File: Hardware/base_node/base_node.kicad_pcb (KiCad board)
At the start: 2 copper layers, 60 x 60 mm, 29 parts, among them J1 IO Interface, J2 RS-422 Connector, J3 Expantion Connector, J4 I2C, J5 24vdc, J6 Encoder 1, J7 Encoder 2, SW1 SW_DIP_x08, U1 CH32X033F8P6, U2 MAX491E, U3 74HC165, U4 MP1584EN_Module

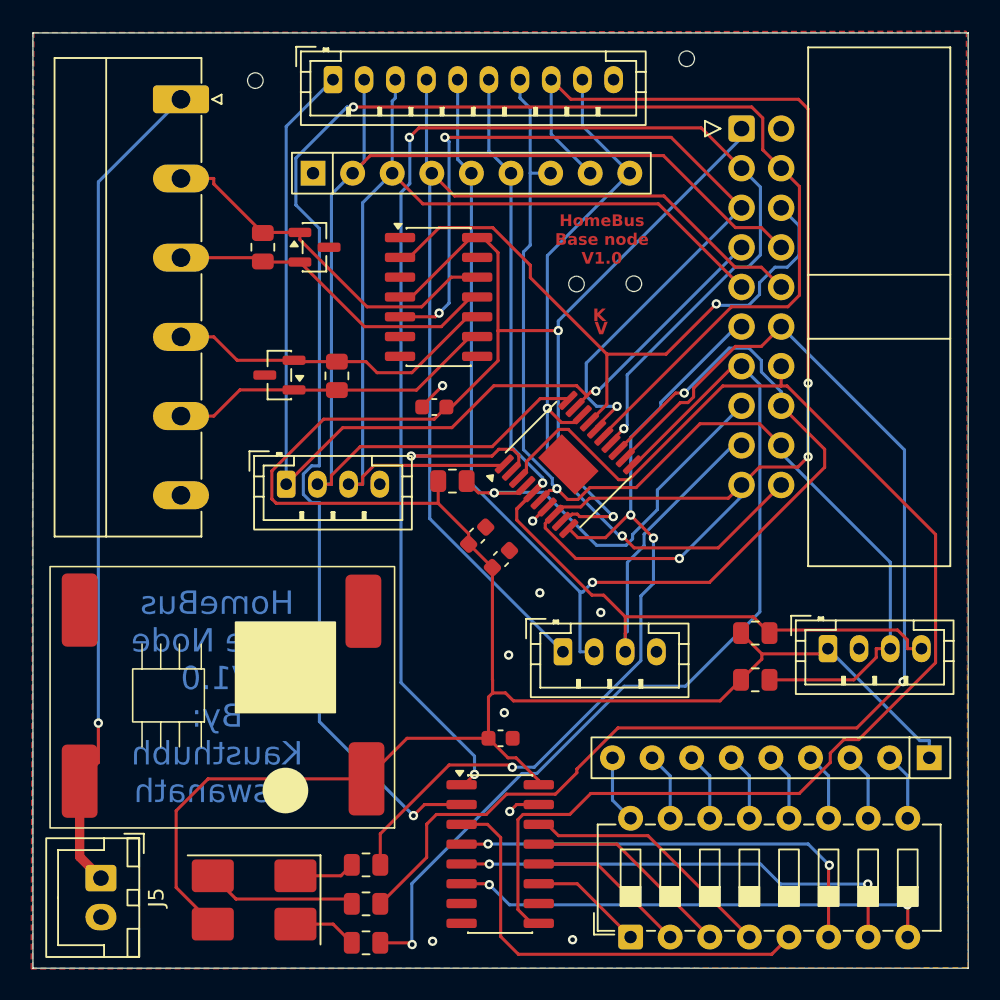
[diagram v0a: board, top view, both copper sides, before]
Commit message: docs: establish hierarchical documentation structure and subsystem guides
- Created root navigation hub README.md linking architecture, subsystems, and components
- Added Hardware Subsystem README (bus topology, 24V power rail, RS-422, SM712 protection, BOM)
- Created Base Node README with pinouts (Dev vs Prod), 3D production renders, and manufacturing specs
- Created Gateway Node README with dual-transceiver room segmentation, EEPROM routing, and dev board
- Created Fan Controller Node README with ZCD optocoupler, isolated gate drive, and anti-stall logic
- Created Expanders README with SMD breakout adapter specs and layout previews
- Created Firmware & Protocol Specification README covering 32-bit addressing, packet formats, and dual-slot OTA
- Synchronized KiCad hardware assets, manufacturing plots, and component libraries
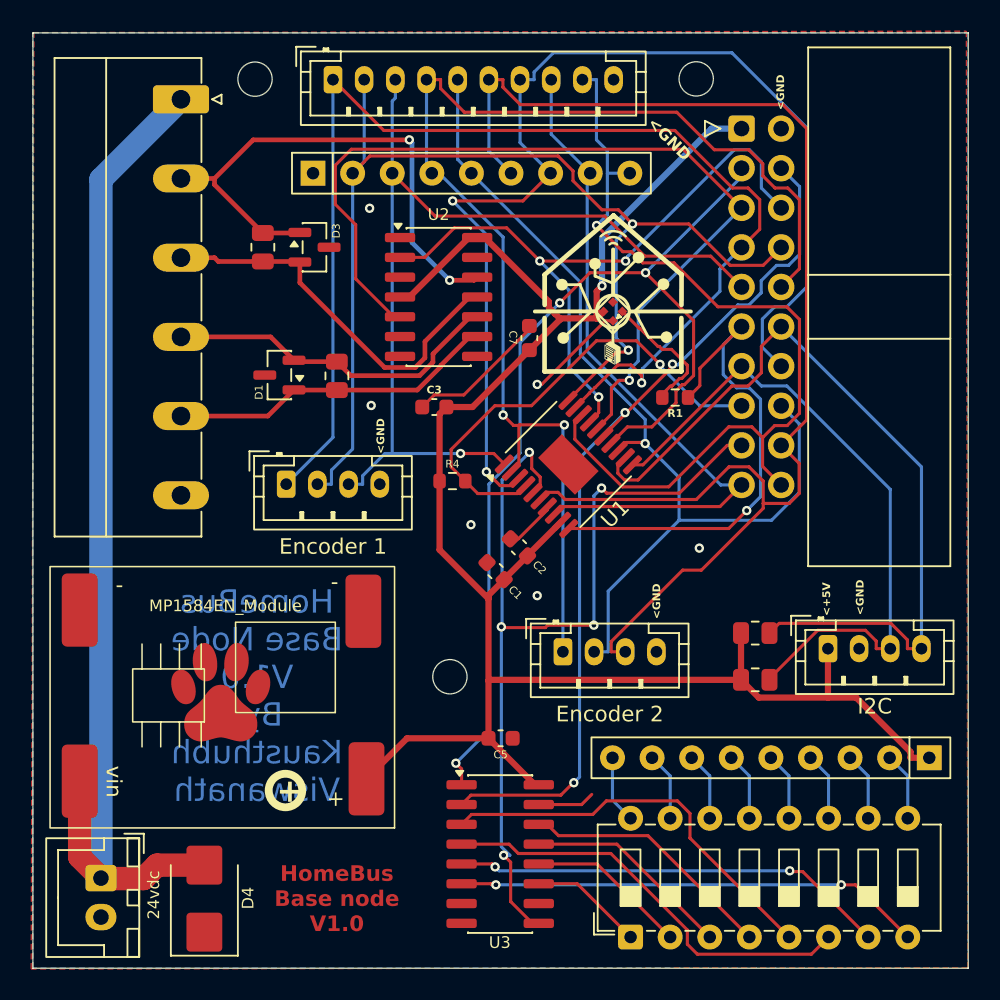
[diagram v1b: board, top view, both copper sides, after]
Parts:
- removed R2, R3: 330Ω, HomeBus:R_0805_2012Metric
- added C7: 100nF, HomeBus:C_0603_1608Metric, F.Cu at (186.3, 115.6)
- added D4: SMBJ26A, Diode_SMD:D_SMB, F.Cu at (165.5, 151.5)
- added Lg1: HomeBus_LOGO, HomeBus:HomeBus_LOGO, F.Cu at (191.7, 113.9)
- added Lg2: OSHW-Logo_5.7x6mm_SilkScreen, Symbol:OSHW-Logo_5.7x6mm_SilkScreen, B.Cu at (168.8, 151.1)
- added Mount1: MountingHole_2.2mm_M2, MountingHole:MountingHole_2.2mm_M2, B.Cu at (168.7, 99.0)
- added Mount2: MountingHole_2.2mm_M2, MountingHole:MountingHole_2.2mm_M2, B.Cu at (197.1, 99.0)
- added Mount3: MountingHole_2.2mm_M2, MountingHole:MountingHole_2.2mm_M2, B.Cu at (181.2, 137.3)
- D2: value LED_RGAB -> WS2812B; footprint HomeBus:Crystal_SMD_0603-4Pin_6.0x3.5mm_HandSoldering -> HomeBus:XINGLIGHT-XL-1010RGBC-WS2812B
- R1, R4: footprint HomeBus:R_0805_2012Metric -> Resistor_SMD:R_0603_1608Metric
- moved D2 44.2 mm to (191.7, 113.9), turned to 45 degrees
- moved R1 35.9 mm to (195.7, 119.4)
- moved C1 2.56 mm to (184.2, 130.5), turned to 135 degrees
- moved C2 1.38 mm to (185.7, 129.0), turned to 135 degrees
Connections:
- net /+24vdc renamed /+24V
- D2 pad 1: Net-(D2-RK) -> +5V
- D2 pad 2: Net-(D2-GK) -> unconnected-(D2-DOUT-Pad2)
- D2 pad 3: +5V -> GND
- D2 pad 4: Net-(D2-BK) -> Net-(D2-DIN)
- J3 pad 12: Net-(J3-Pin_12) -> /SCL
- J3 pad 13: Net-(J3-Pin_13) -> /SDA
- J3 pad 14: Net-(J3-Pin_14) -> Net-(J1-Pin_7)
- J3 pad 17: Net-(J1-Pin_6) -> Net-(J3-Pin_17)
- J3 pad 18: Net-(J1-Pin_7) -> Net-(J1-Pin_6)
- J4 pad 3: Net-(J1-Pin_7) -> /SDA
- J4 pad 4: Net-(J1-Pin_6) -> /SCL
- R1 pad 2: Net-(D2-RK) -> Net-(D2-DIN)
- R7 pad 2: Net-(J1-Pin_7) -> /SDA
- R8 pad 2: Net-(J1-Pin_6) -> /SCL
- U1 pad 11: Net-(J3-Pin_13) -> /SDA
- U1 pad 12: Net-(J3-Pin_12) -> /SCL
- U1 pad 3: Net-(J3-Pin_14) -> Net-(J1-Pin_7)
- U1 pad 5: Net-(J1-Pin_6) -> Net-(J3-Pin_17)
- U1 pad 6: Net-(J1-Pin_7) -> Net-(J1-Pin_6)
- U3 pad 9: Net-(J3-Pin_14) -> Net-(J3-Pin_17)
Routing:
- net Net-(J3-Pin_14): track 84.4 -> 0.00 mm
- net Net-(J3-Pin_12): track 80.7 -> 0.00 mm, vias 1 -> 0
- net Net-(J3-Pin_13): track 61.4 -> 0.00 mm, vias 1 -> 0
- net Net-(J3-Pin_17): track 0.00 -> 61.2 mm, vias 0 -> 5
- net Net-(J3-Pin_4): track 110.4 -> 57.0 mm, vias 2 -> 3
- net /SCL: track 0.00 -> 52.3 mm
- net +5V: track 172.0 -> 123.7 mm, vias 2 -> 1
- net /SDA: track 0.00 -> 42.5 mm
- net Net-(J1-Pin_8): track 82.0 -> 44.8 mm, vias 3 -> 0
- net Net-(J3-Pin_3): track 89.4 -> 64.8 mm
- net Net-(J3-Pin_11): track 53.7 -> 32.0 mm, vias 3 -> 1
- net Net-(J1-Pin_5): track 80.6 -> 61.8 mm, vias 2 -> 1
- net GND: track 5.26 -> 22.7 mm, vias 9 -> 6
- net Net-(J1-Pin_1): track 64.3 -> 78.8 mm
- net /+24V: track 53.2 -> 65.9 mm, vias 1 -> 0
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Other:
- outline, holes or cut-outs redrawn
- board text added: "<+5V"
- board text added: "<GND"
- board text removed: "K"
- board text removed: "V"
